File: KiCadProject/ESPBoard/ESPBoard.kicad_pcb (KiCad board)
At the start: 2 copper layers, 45 x 45 mm, 69 parts, among them J201 Conn_02x05, J202 Conn_01x02, J203 Conn_02x05, J204 JST_SM04B, J205 DNP, J206 1x05 female, J207 JST_SM04B, SW301 SW_Push, SW302 SW_Push, U301 ESP32-S3-WROOM-1

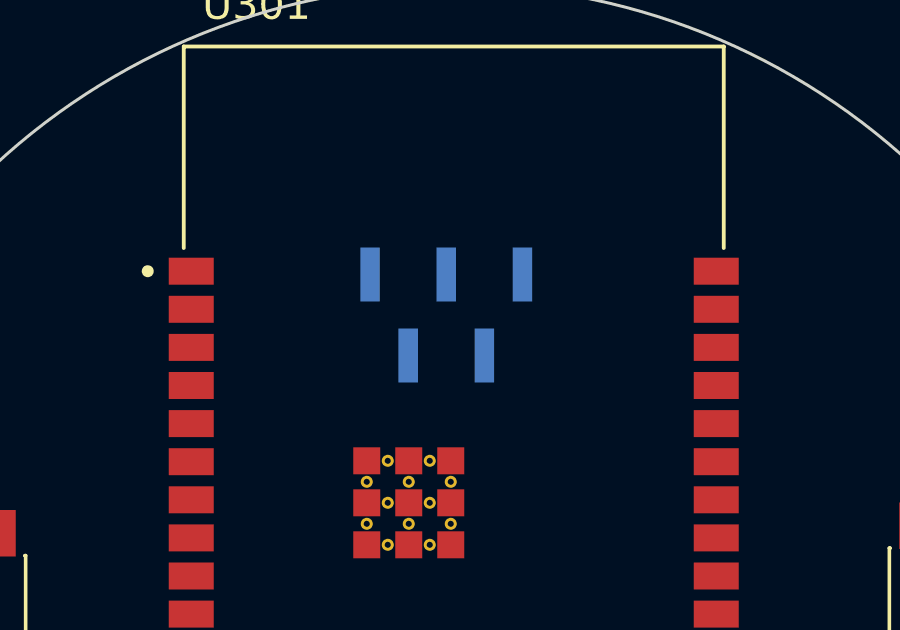
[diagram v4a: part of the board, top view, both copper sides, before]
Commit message: Routed Bat management (replaced TUSB because it physically can't be routed with constraints)
Signed-off-by: Eldalote.Electronics <Eldalote.Electronics@gmail.com>
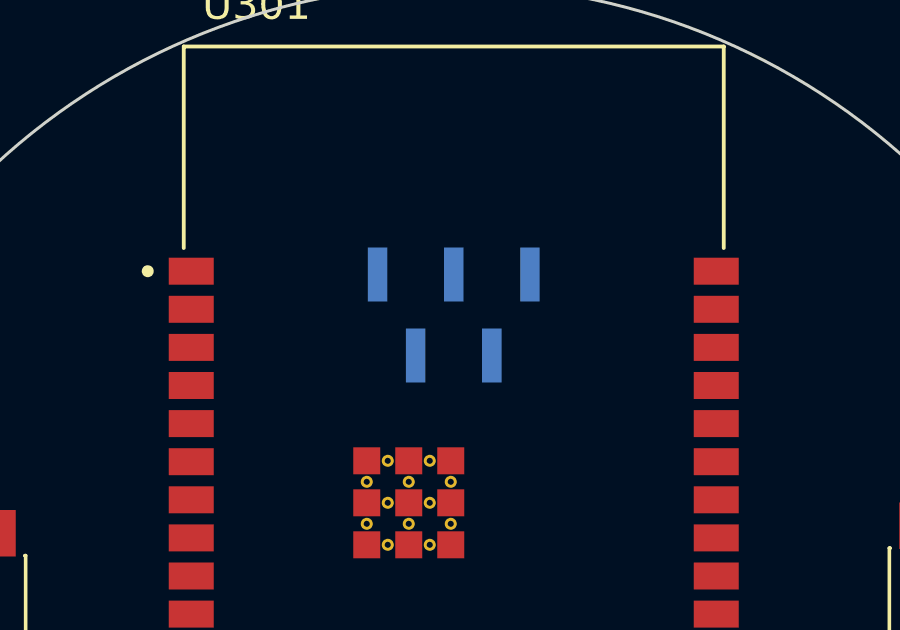
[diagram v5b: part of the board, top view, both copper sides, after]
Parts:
- moved J206 0.25 mm to (150.0, 88.5)
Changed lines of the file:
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@@
   )
   (footprint "Connector_PinSocket_1.27mm:PinSocket_1x05_P1.27mm_Vertical_SMD_Pin1Left" (layer "B.Cu")
-    (at 149.75 88.5 -90)
+    (at 150 88.5 -90)
     (descr "surface-mounted straight socket strip, 1x05, 1.27mm pitch, single row, style 1 (pin 1 left) (https://gct.co/pdfjs/web/viewer.html?file=/Files/Drawings/BD075.pdf&t=1511594726925), script generated")
     (tags "Surface mounted socket strip SMD 1x05 1.27mm single row style1 pin1 left")

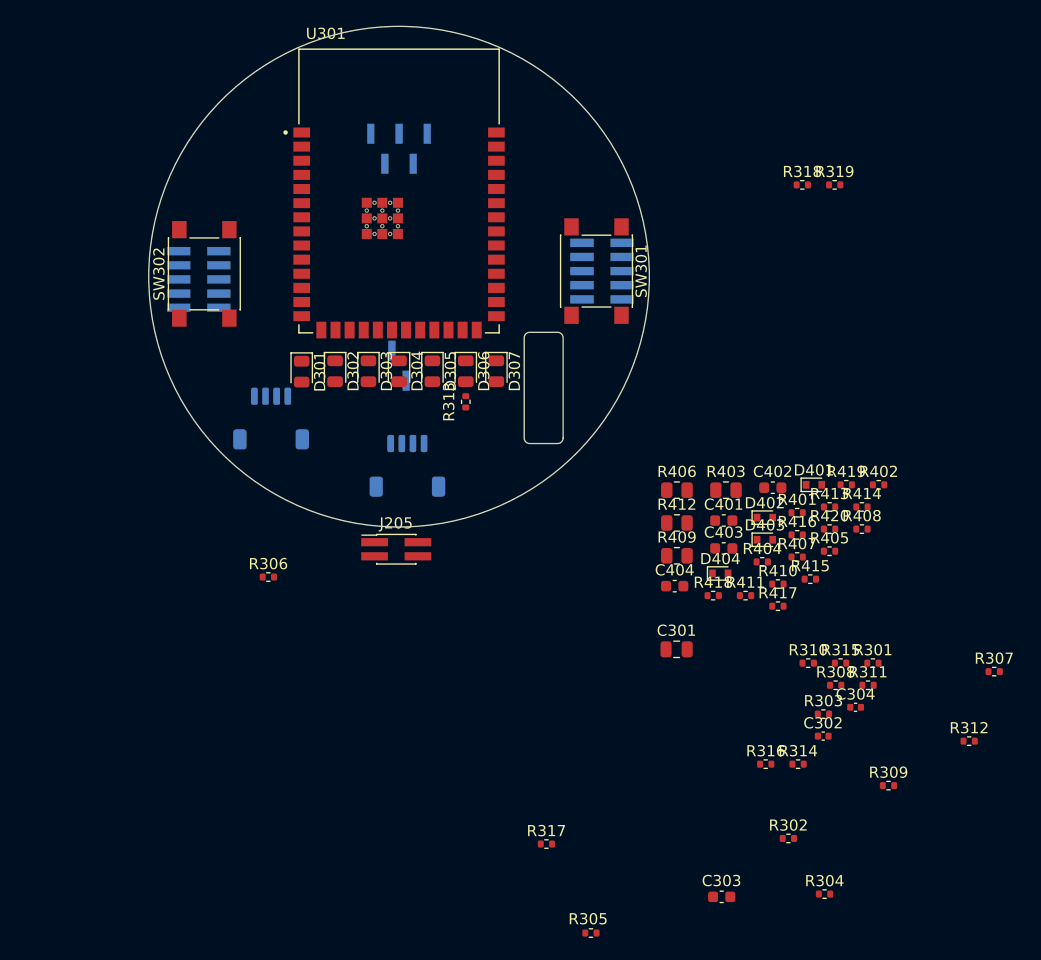
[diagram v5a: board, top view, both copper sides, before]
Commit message: Finished v0.1 of BatMan PCB, started layout of ESP PCB
Signed-off-by: Eldalote.Electronics <Eldalote.Electronics@gmail.com>
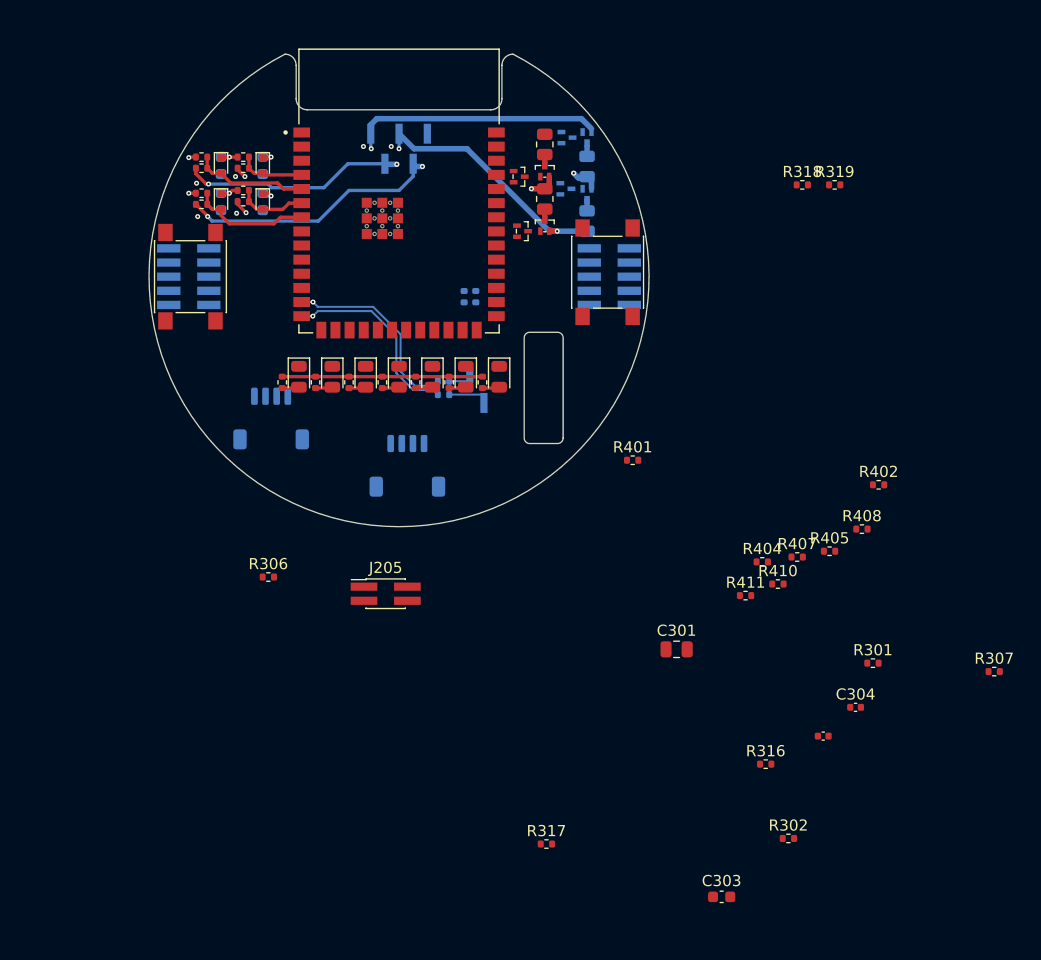
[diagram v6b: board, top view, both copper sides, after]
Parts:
- added Q401: NFET_Gatenames, Eldalote-footprints:SC-89(GSD), B.Cu at (165.1, 87.5)
- added Q402: PMOS_Gatenames, Eldalote-footprints:SOT-723(GSD), B.Cu at (166.9, 87.5)
- added Q403: NFET_Gatenames, Eldalote-footprints:SC-89(GSD), B.Cu at (165.0, 92.1)
- added Q404: PMOS_Gatenames, Eldalote-footprints:SOT-723(GSD), B.Cu at (166.9, 92.6)
- added Q405: NFET_Gatenames, Eldalote-footprints:SC-89(GSD), F.Cu at (161.1, 95.9)
- added Q406: PMOS_Gatenames, Eldalote-footprints:SOT-723(GSD), F.Cu at (163.1, 95.4)
- added Q407: NFET_Gatenames, Eldalote-footprints:SC-89(GSD), F.Cu at (160.8, 91.0)
- added Q408: PMOS_Gatenames, Eldalote-footprints:SOT-723(GSD), F.Cu at (163.1, 90.5)
- C401, C402, C403, C404, R303, R304, R305, R315, R403, R406: moved to B.Cu
- moved R414 65.7 mm to (132.2, 92.5), turned to 180 degrees
- moved R417 65.1 mm to (132.2, 90.2)
- moved R309 63.0 mm to (142.5, 109.5), turned to -90 degrees
- moved R413 62.7 mm to (132.2, 93.5)
- moved R420 62.4 mm to (136.0, 89.2), turned to 180 degrees
- moved R415 61.2 mm to (136.0, 93.2)
- moved R419 61.2 mm to (136.0, 90.2)
- moved R418 60.6 mm to (132.2, 89.2), turned to 180 degrees
- moved D403 59.3 mm to (134.0, 90.0), turned to -90 degrees
- moved R312 59.3 mm to (151.5, 109.5), turned to -90 degrees
- moved D401 59.1 mm to (134.0, 93.2), turned to -90 degrees
- moved R416 58.6 mm to (136.0, 92.2), turned to 180 degrees
- moved R305 58.1 mm to (156.9, 101.8), turned to 90 degrees
- moved R304 57.4 mm to (154.0, 109.4)
- moved C403 56.8 mm to (134.0, 90.0), turned to 90 degrees
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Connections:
- J201 pad 9: GND -> USBPD_PTN_ID
- R403 pad 1: Net-(Q402-PadD) -> /P4 Batsense-Balancing/C4L
- R406 pad 1: Net-(Q404-PadD) -> /P4 Batsense-Balancing/C3L
- R409 pad 1: Net-(Q406-PadD) -> /P4 Batsense-Balancing/C2L
- R412 pad 1: Net-(Q408-PadD) -> /P4 Batsense-Balancing/C1L
- U301 pad 4: Cell1ADC -> Cell4ADC
- U301 pad 5: Cell2ADC -> Cell3ADC
- U301 pad 6: Cell3ADC -> Cell2ADC
- U301 pad 7: Cell4ADC -> Cell1ADC
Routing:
- net Cell2: track 0.00 -> 40.0 mm, vias 0 -> 3
- net Cell3: track 0.00 -> 40.0 mm, vias 0 -> 3
- net Cell1: track 0.00 -> 37.0 mm, vias 0 -> 3
- net Cell4: track 0.00 -> 36.0 mm, vias 0 -> 2
- net +3.3V: track 0.00 -> 18.0 mm
- net /P3 ESP32/USB_D+: track 0.00 -> 17.5 mm, vias 0 -> 1
- net /P3 ESP32/USB_D-: track 0.00 -> 17.5 mm, vias 0 -> 1
- net Cell1ADC: track 0.00 -> 10.8 mm
- net Cell3ADC: track 0.00 -> 10.3 mm
- net GND: track 0.00 -> 9.17 mm, vias 0 -> 12
- net Cell2ADC: track 0.00 -> 6.26 mm
- net Cell4ADC: track 0.00 -> 5.99 mm
- net C_USB_D+: track 0.00 -> 3.85 mm
- net C_USB_D-: track 0.00 -> 2.70 mm
- net /P3 ESP32/L6a: track 0.00 -> 1.53 mm
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- added copper zone on In1.Cu, net GND
- added copper zone on In3.Cu, net GND
- added copper zone on In4.Cu, net GND
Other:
- board size 45 x 45 mm -> 44.9 x 42.5 mm
- copper layers 2 -> 6

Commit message: Finished V0.1 of ESP PCB
Signed-off-by: Eldalote.Electronics <Eldalote.Electronics@gmail.com>
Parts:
- C301, R306, R307, R316, R317, R318, R319, R401, R402, R404, R405, R407, R408, R410, R411: moved to B.Cu
- Q401, Q402, Q403, Q404, R403, R406: moved to F.Cu
- moved C303 82.0 mm to (135.7, 86.1), turned to 90 degrees
- moved R301 73.4 mm to (137.1, 86.7), turned to -90 degrees
- moved C302 73.2 mm to (139.2, 86.8), turned to 90 degrees
- moved R307 69.2 mm to (144.0, 100.2), turned to 90 degrees
- moved R316 56.8 mm to (146.5, 100.2), turned to -90 degrees
- moved C301 55.4 mm to (143.8, 87.8), turned to 90 degrees
- moved R317 54.6 mm to (143.0, 100.2), turned to -90 degrees
- moved R302 48.5 mm to (170.4, 104.3), turned to 90 degrees
- moved R410 46.7 mm to (161.5, 86.8), turned to -90 degrees
- moved R411 45.3 mm to (164.0, 86.8), turned to 180 degrees
- moved C304 42.8 mm to (165.6, 104.2), turned to 90 degrees
- moved R407 41.5 mm to (161.7, 91.4), turned to -90 degrees
- moved R408 41.2 mm to (164.0, 92.1), turned to 180 degrees
- moved R402 40.0 mm to (166.3, 89.0)
- moved R405 36.9 mm to (166.6, 95.1), turned to -90 degrees
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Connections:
- C301 pad 1: +3.3V -> +3V3
- C302 pad 1: +3.3V -> +3V3
- R301 pad 1: +3.3V -> +3V3
- R302 pad 1: +3.3V -> +3V3
- R308 pad 1: +3.3V -> +3V3
- R309 pad 1: +3.3V -> +3V3
- R310 pad 1: +3.3V -> +3V3
- R311 pad 1: +3.3V -> +3V3
- R312 pad 1: +3.3V -> +3V3
- R313 pad 1: +3.3V -> +3V3
- R314 pad 1: +3.3V -> +3V3
- R315 pad 1: +3.3V -> +3V3
- R316 pad 1: +3.3V -> +3V3
- R317 pad 1: +3.3V -> +3V3
- R318 pad 1: +3.3V -> +3V3
- R319 pad 1: +3.3V -> +3V3
- U301 pad 10: unconnected-(U301-Pad10) -> BQ_IBAT
- U301 pad 12: BQ_CMPOUT -> unconnected-(U301-Pad12)
- U301 pad 17: unconnected-(U301-Pad17) -> BQ_EN_OTG
- U301 pad 18: unconnected-(U301-Pad18) -> MAINLED_PWM
- U301 pad 19: unconnected-(U301-Pad19) -> MAINLED_nFTL
- U301 pad 2: +3.3V -> +3V3
- U301 pad 20: unconnected-(U301-Pad20) -> /P3 ESP32/LED0
- U301 pad 21: unconnected-(U301-Pad21) -> /P3 ESP32/LED1
- U301 pad 22: unconnected-(U301-Pad22) -> /P3 ESP32/LED2
- U301 pad 23: unconnected-(U301-Pad23) -> /P3 ESP32/LED3
- U301 pad 24: unconnected-(U301-Pad24) -> /P3 ESP32/LED4
- U301 pad 25: unconnected-(U301-Pad25) -> /P3 ESP32/LED5
- U301 pad 28: unconnected-(U301-Pad28) -> /P3 ESP32/LED6
- U301 pad 29: unconnected-(U301-Pad29) -> I2C_SDA
- U301 pad 30: unconnected-(U301-Pad30) -> I2C_SCL
- U301 pad 31: unconnected-(U301-Pad31) -> USBPD_INT_N
- U301 pad 32: unconnected-(U301-Pad32) -> BQ_CHRG_OK
- U301 pad 33: unconnected-(U301-Pad33) -> USBPD_PTN_ID
- U301 pad 34: unconnected-(U301-Pad34) -> Cell3Balance
- U301 pad 35: unconnected-(U301-Pad35) -> Cell4Balance
- U301 pad 38: BQ_IADPT -> Cell2Balance
- U301 pad 39: BQ_IBAT -> Cell1Balance
- U301 pad 8: unconnected-(U301-Pad8) -> BQ_CMPOUT
- U301 pad 9: unconnected-(U301-Pad9) -> BQ_IADPT
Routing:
- net +3V3: track 0.00 -> 136.3 mm, vias 0 -> 11
- net GND: track 9.17 -> 61.3 mm, vias 12 -> 147
- net UART_RXDO: track 0.00 -> 36.2 mm, vias 0 -> 2
- net I2C_SCL: track 0.00 -> 35.3 mm, vias 0 -> 1
- net UART_TXDO: track 0.00 -> 35.2 mm, vias 0 -> 2
- net I2C_SDA: track 0.00 -> 33.3 mm, vias 0 -> 2
- net /P3 ESP32/CHIP_PU: track 0.00 -> 32.6 mm
- net BQ_EN_OTG: track 0.00 -> 20.0 mm, vias 0 -> 1
- net +3.3V: track 18.0 -> 0.00 mm
- net /P3 ESP32/BOOT/USER1: track 0.00 -> 14.4 mm
- net BQ_CMPOUT: track 0.00 -> 13.1 mm, vias 0 -> 1
- net Cell3Balance: track 0.00 -> 12.9 mm, vias 0 -> 1
- net MAINLED_nFTL: track 0.00 -> 12.7 mm, vias 0 -> 1
- net MAINLED_PWM: track 0.00 -> 12.6 mm, vias 0 -> 1
- net USBPD_PTN_ID: track 0.00 -> 12.6 mm, vias 0 -> 1
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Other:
- outline, holes or cut-outs redrawn
- board text added: "01"
- board text added: "S1"
- board text added: "S2"
- board text added: "S3"

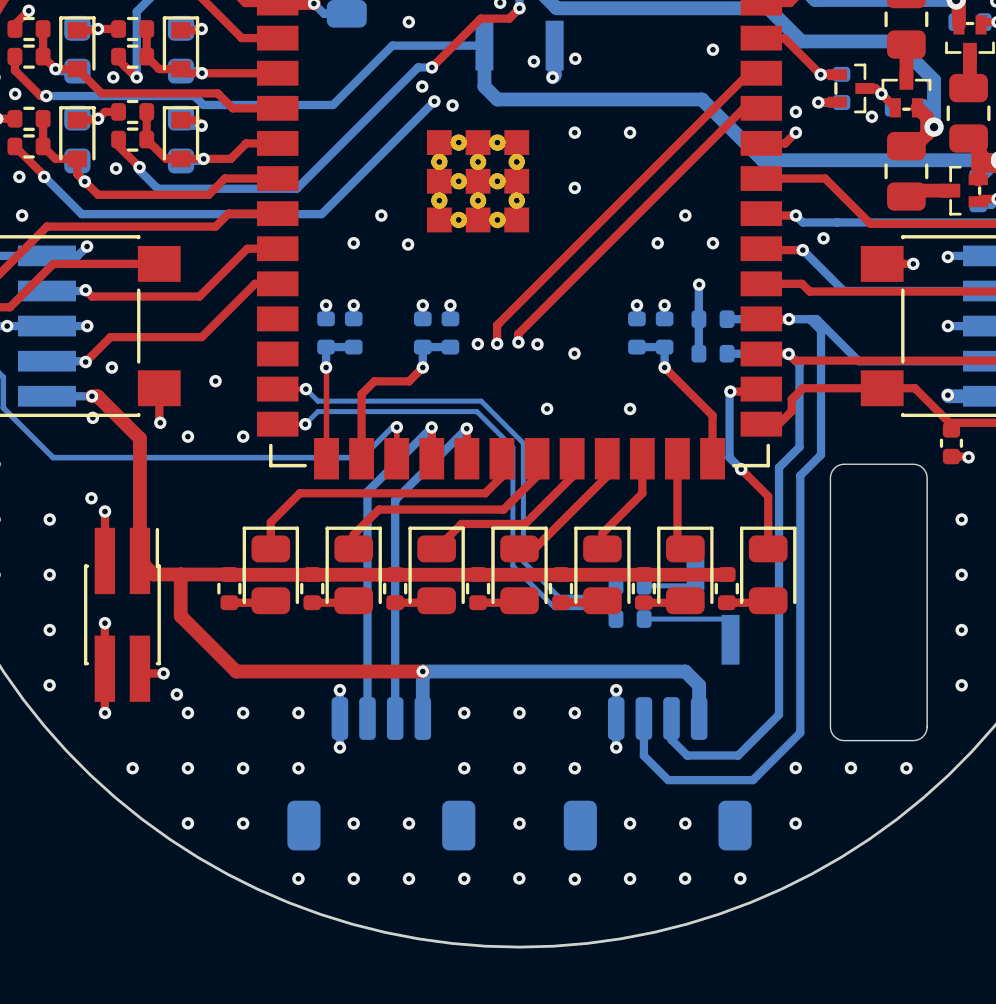
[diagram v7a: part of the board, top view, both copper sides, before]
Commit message: All PCB's should be done. Do a final check before ordering.
Signed-off-by: Eldalote.Electronics <Eldalote.Electronics@gmail.com>
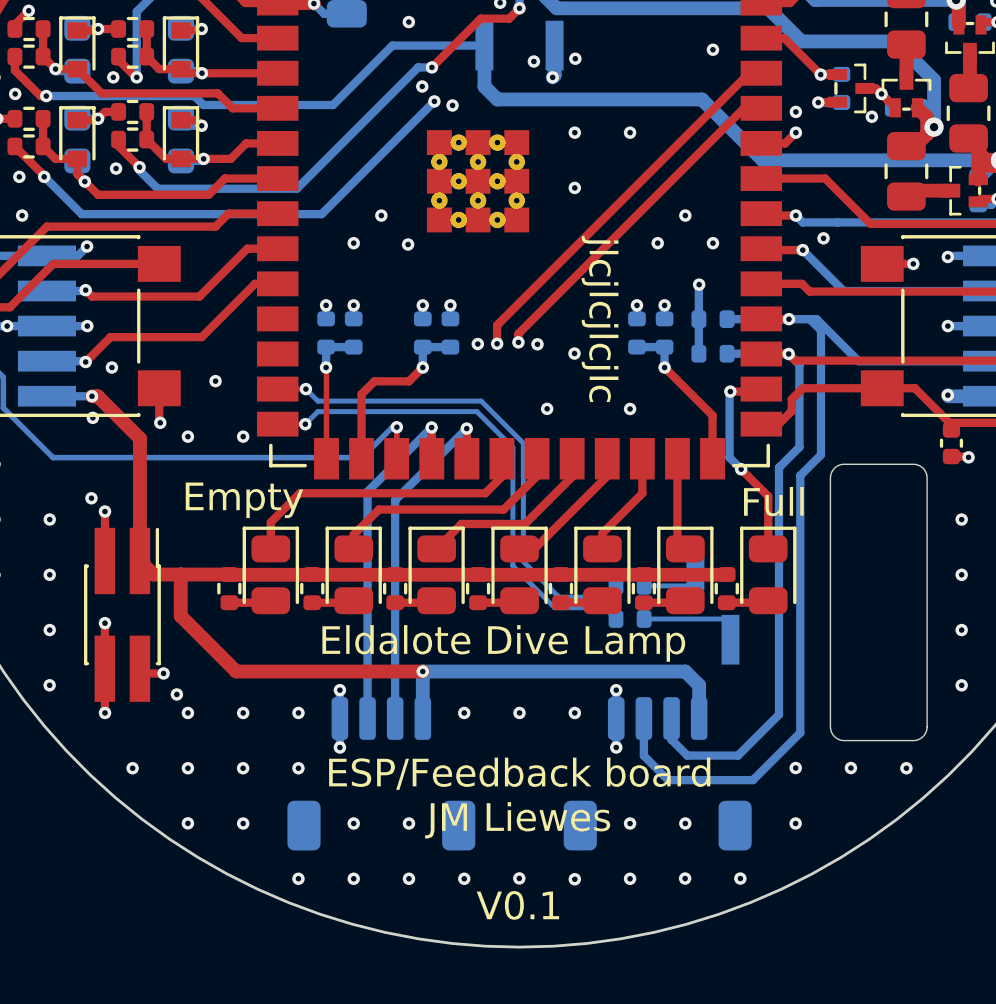
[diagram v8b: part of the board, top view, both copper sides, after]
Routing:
- net GND: vias 147 -> 143
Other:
- board text added: "ESP/Feedback board JM Liewes"
- board text added: "Eldalote Dive Lamp"
- board text added: "Empty"
- board text added: "Full"
- board text added: "V0.1"
- board text added: "jlcjlcjlcjlc"
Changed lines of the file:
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@@
     (pad "4" smd rect (at 1.95 0.635 270) (size 2.4 0.74) (layers "F.Cu" "F.Paste" "F.Mask")
       (net 21 "GND") (pinfunction "Pin_4") (pintype "passive"))
-    (model "${KICAD6_3DMODEL_DIR}/Connector_PinHeader_1.27mm.3dshapes/PinHeader_2x02_P1.27mm_Vertical_SMD.wrl"
+    (model "${KICAD6_3DMODEL_DIR}/Connector_PinHeader_1.27mm.3dshapes/PinHeader_2x02_P1.27mm_Vertical_SMD.wrl" hide
       (offset (xyz 0 0 0))
       (scale (xyz 1 1 1))
@@
   (gr_text "01" (at 147 102.5) (layer "B.SilkS")
     (effects (font (size 1 1) (thickness 0.16)) (justify mirror))
+  )
+  (gr_text "ESP/Feedback board\nJM Liewes" (at 150 117) (layer "F.SilkS")
+    (effects (font (size 1 1) (thickness 0.16)))
+  )
+  (gr_text "Eldalote Dive Lamp" (at 149.4 111.4) (layer "F.SilkS")
+    (effects (font (size 1 1) (thickness 0.16)))
+  )
+  (gr_text "Empty" (at 140 106.2) (layer "F.SilkS")
+    (effects (font (size 1 1) (thickness 0.16)))
+  )
+  (gr_text "V0.1" (at 150 121) (layer "F.SilkS")
+    (effects (font (size 1 1) (thickness 0.16)))
+  )
+  (gr_text "Full" (at 159.2 106.4) (layer "F.SilkS")
+    (effects (font (size 1 1) (thickness 0.16)))
+  )
+  (gr_text "jlcjlcjlcjlc" (at 153 99.8 -90) (layer "F.SilkS")
+    (effects (font (size 1 1) (thickness 0.16)))
   )
   (segment (start 129.657831 91.436895) (end 130.0386 90.583361) (width 0.3) (layer "F.Cu") (net 1))
@@
   (via (at 131.46 100) (size 0.45) (drill 0.2) (layers "F.Cu" "B.Cu") (net 21))
   (via (at 157 97) (size 0.45) (drill 0.2) (layers "F.Cu" "B.Cu") (free) (net 21))
-  (via (at 152 116) (size 0.45) (drill 0.2) (layers "F.Cu" "B.Cu") (free) (net 21))
   (via (at 134.75 89.25) (size 0.45) (drill 0.2) (layers "F.Cu" "B.Cu") (net 21))
   (via (at 151.989892 100.99336) (size 0.45) (drill 0.2) (layers "F.Cu" "B.Cu") (free) (net 21))
@@
   (via (at 139 83) (size 0.45) (drill 0.2) (layers "F.Cu" "B.Cu") (free) (net 21))
   (via (at 134.56 103.32) (size 0.45) (drill 0.2) (layers "F.Cu" "B.Cu") (net 21))
-  (via (at 148 116) (size 0.45) (drill 0.2) (layers "F.Cu" "B.Cu") (free) (net 21))
   (via (at 139 82) (size 0.45) (drill 0.2) (layers "F.Cu" "B.Cu") (free) (net 21))
   (via (at 135.25 101.5) (size 0.45) (drill 0.2) (layers "F.Cu" "B.Cu") (net 21))
@@
   (via (at 135.4 94.3) (size 0.45) (drill 0.2) (layers "F.Cu" "B.Cu") (net 21))
   (via (at 155 87) (size 0.45) (drill 0.2) (layers "F.Cu" "B.Cu") (free) (net 21))
-  (via (at 150 118) (size 0.45) (drill 0.2) (layers "F.Cu" "B.Cu") (free) (net 21))
   (via (at 136 116) (size 0.45) (drill 0.2) (layers "F.Cu" "B.Cu") (free) (net 21))
   (via (at 152 114) (size 0.45) (drill 0.2) (layers "F.Cu" "B.Cu") (free) (net 21))
@@
   (via (at 138.999999 101.99201) (size 0.45) (drill 0.2) (layers "F.Cu" "B.Cu") (free) (net 21))
   (via (at 159.5 86) (size 0.45) (drill 0.2) (layers "F.Cu" "B.Cu") (net 21))
-  (via (at 150 116) (size 0.45) (drill 0.2) (layers "F.Cu" "B.Cu") (free) (net 21))
   (via (at 131 105) (size 0.45) (drill 0.2) (layers "F.Cu" "B.Cu") (free) (net 21))
   (via (at 131 109) (size 0.45) (drill 0.2) (layers "F.Cu" "B.Cu") (free) (net 21))
